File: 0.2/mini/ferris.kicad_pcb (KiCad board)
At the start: 2 copper layers, 208.8 x 86.8 mm, 114 parts, among them J1 USB C, K0_0 KEYSW, K0_1 KEYSW, K0_2 KEYSW, K0_3 KEYSW, K0_4 KEYSW, K0_5 KEYSW, K0_6 KEYSW, K0_7 KEYSW, K0_8 KEYSW, K0_9 KEYSW, K1_0 KEYSW, K1_1 KEYSW, K1_2 KEYSW, K1_3 KEYSW, K1_4 KEYSW, K1_5 KEYSW, K1_6 KEYSW, K1_7 KEYSW, K1_8 KEYSW, K1_9 KEYSW, K2_0 KEYSW, K2_1 KEYSW, K2_2 KEYSW, K2_3 KEYSW, K2_4 KEYSW, K2_5 KEYSW, K2_6 KEYSW, K2_7 KEYSW, K2_8 KEYSW, K2_9 KEYSW, K3_3 KEYSW, K3_4 KEYSW, K3_5 KEYSW, K3_6 KEYSW, Q1 DTC123J, SW1 SW_PUSH, U1 STM32F072CBTx, U2 MCP23017_SO, U3 MCP1700-3302E_SOT23, U4 SRV05-4

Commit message: Remove last few references to ferris.pretty and the entire directory
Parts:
- removed the mouse-bite-2mm-slot at (132.8, 30.0)
- removed the mouse-bite-2mm-slot at (103.2, 30.0)
- added mouse-bite-2mm-slot: VAL**, panelization:mouse-bite-2mm-slot-with-space-for-track, F.Cu at (132.8, 30.0)
- added mouse-bite-2mm-slot: VAL**, panelization:mouse-bite-2mm-slot-with-space-for-track, F.Cu at (103.2, 30.0)
- G*** (x2): footprint ferris:ducking_ferris_pad -> copper_pads:ferris_low
- REF**: footprint ferris:silk_pg1232_schematic -> silkscreens:pg1232_schematic
- REF**: footprint ferris:silk_pg2132_top -> silkscreens:pg1232_top
- REF**: footprint ferris:silk_pg1232_bottom -> silkscreens:pg1232_bottom
- REF**: footprint ferris:silk_pg1232_right -> silkscreens:pg1232_right
- REF**: footprint ferris:silk_pg1232_left -> silkscreens:pg1232_left
- REF**: footprint ferris:silk_pg1232_footprint -> silkscreens:pg1232_footprint
- REF**: footprint ferris:silk_pg1232_side -> silkscreens:pg1232_side
- mouse-bite-2mm-slot: footprint ferris:mouse-bite-2mm-slot-with-space-for-track -> panelization:mouse-bite-2mm-slot-with-space-for-track

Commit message: 0.2/mini: Add human readable "Part Name" field
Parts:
- C12, C13: value 0.1u -> 0.1uF
- D0_0, D0_1, D0_2, D0_3, D0_4, D0_5, D0_6, D0_7, D0_8, D0_9, D1_0, D1_1, D1_2, D1_3, D1_4, D1_5, D1_6, D1_7, D1_8, D1_9, D2_0, D2_1, D2_2, D2_3, D2_4, D2_5, D2_6, D2_7, D2_8, D2_9, D3, D3_3, D3_4, D3_5, D3_6: value D -> 1N4148W
- J1: value USB C -> TYPE-C-31-M-12
- Jack0, Jack1: value TRRS -> PJ-320A
- Q1: value DTC123J -> PDTC123JT,215
- R1, R2: value 5.1K -> 5.1kΩ
- R3, R4, R5: value 100k -> 100kΩ
- R6: value 10k -> 10kΩ
- R7, R8: value 4.7k -> 4.7kΩ
- SW1: value SW_PUSH -> B3U-1000P
- U1: value STM32F072CBTx -> STM32F072CBT6
- U2: value MCP23017_SO -> MCP23017-E/SO
- U3: value MCP1700-3302E_SOT23 -> MCP1700T-3302E/TT
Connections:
- J1 pad A8: (no net) -> Net-(J1-PadA8)
- J1 pad B8: (no net) -> Net-(J1-PadB8)
- U2 pad 11: (no net) -> Net-(U2-Pad11)
- U2 pad 14: (no net) -> Net-(U2-Pad14)
- U2 pad 19: (no net) -> Net-(U2-Pad19)
- U2 pad 20: (no net) -> Net-(U2-Pad20)
- U2 pad 26: (no net) -> Net-(U2-Pad26)
- U2 pad 27: (no net) -> Net-(U2-Pad27)
- U2 pad 28: (no net) -> Net-(U2-Pad28)
- U2 pad 5: (no net) -> Net-(U2-Pad5)
- U2 pad 6: (no net) -> Net-(U2-Pad6)
- U2 pad 7: (no net) -> Net-(U2-Pad7)
- U2 pad 8: (no net) -> Net-(U2-Pad8)

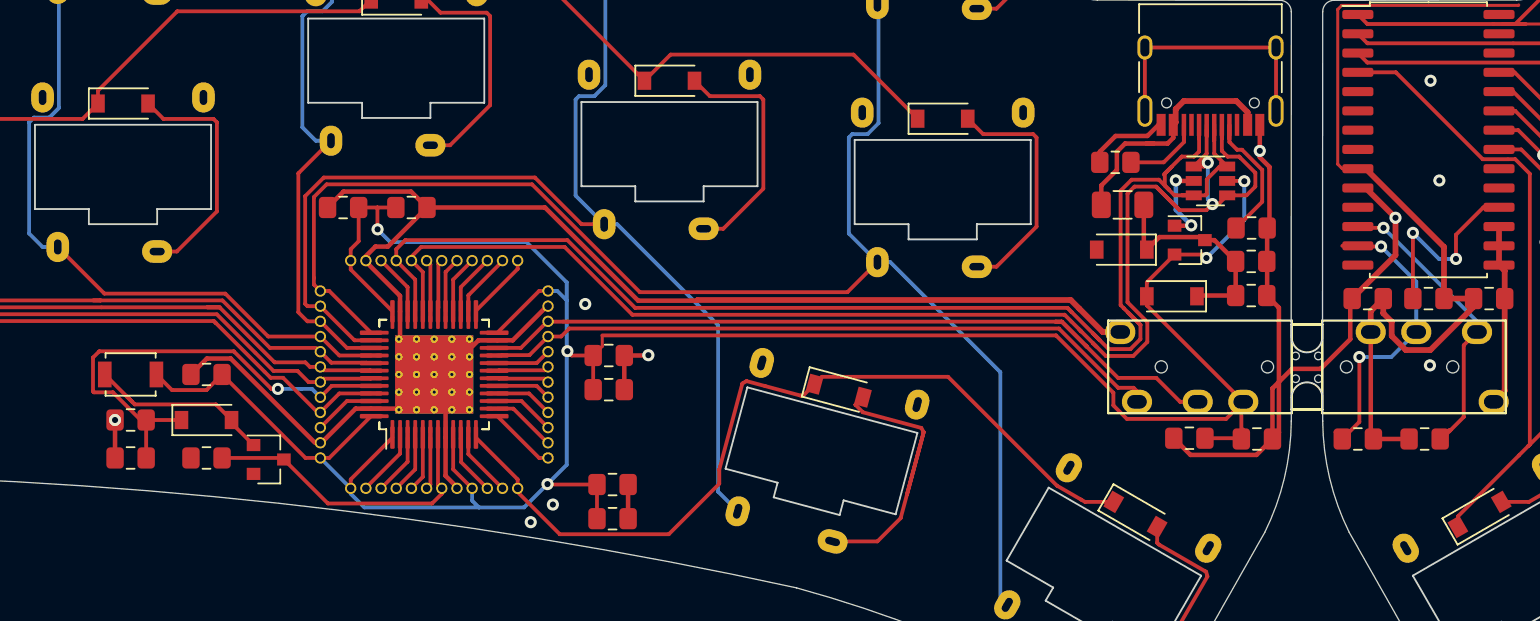
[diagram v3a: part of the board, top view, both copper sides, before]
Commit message: Ferris mini: Update PCB to ease case design
Perform a number of small changes to allow for creation of a symmetrical
switch plate that can cover the MCU area and leave the USB area exposed.
Also move components a bit further from the switches to avoid very slim
parts of the case.

* Move reset button to USB area
* Layout the USB area in a more compact way
* Bring MCU's decoupling capacitors closer to the MCU
* Bring Components under the Jack plugs closer to each other
* Reroute traces accordingly
* Update version to 0.2.1 to reflect the change (silk and mini card)
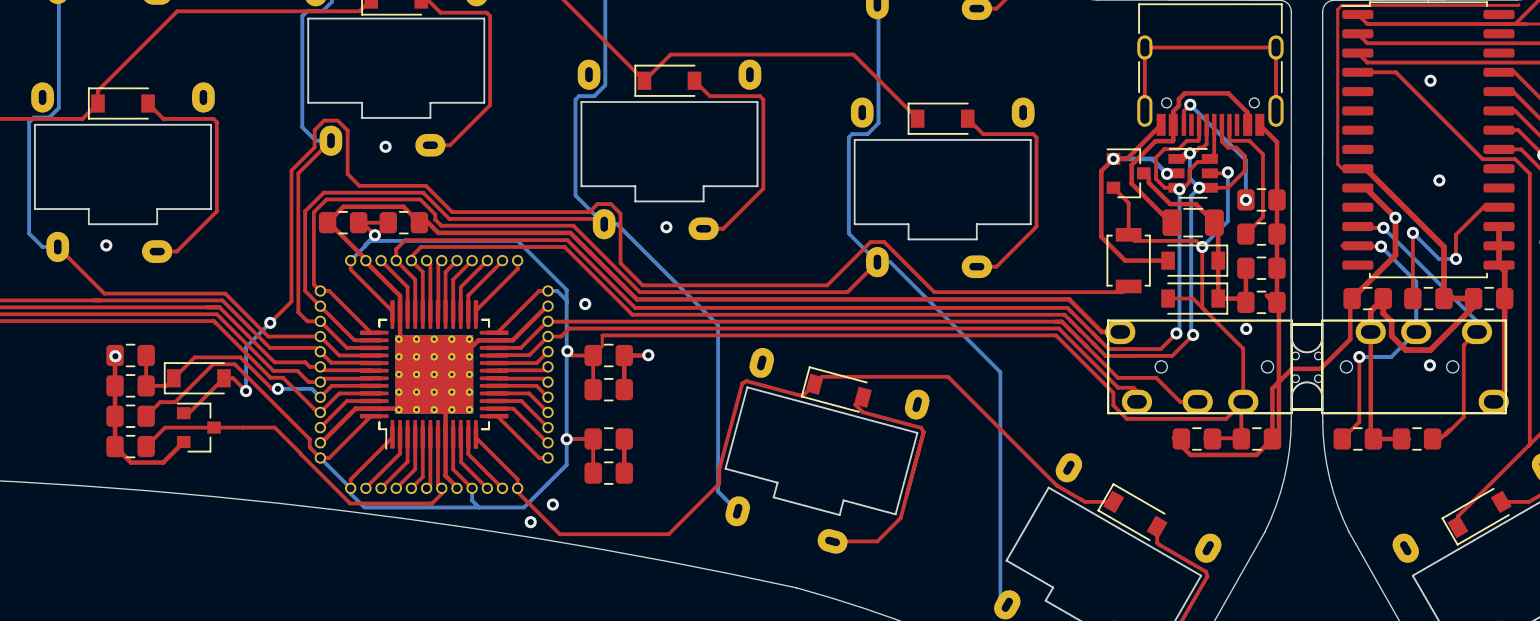
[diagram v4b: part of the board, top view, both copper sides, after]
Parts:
- moved SW1 66.2 mm to (106.2, 69.0), turned to 270 degrees
- moved R2 9.94 mm to (115.0, 65.0), turned to 180 degrees
- moved R5 6.75 mm to (40.5, 75.2)
- moved U3 5.96 mm to (106.2, 63.2)
- moved C9 5.71 mm to (40.5, 79.2)
- moved Q1 5.06 mm to (45.0, 80.0)
- moved C4 5.06 mm to (40.5, 81.2)
- moved F1 4.80 mm to (110.5, 66.5)
- moved D1 4.76 mm to (110.5, 69.0)
- moved C7 3.01 mm to (72.0, 80.8)
- moved C8 3.01 mm to (72.0, 83.0)
- moved D3 2.80 mm to (45.0, 76.8)
- moved C3 2.25 mm to (40.5, 77.2)
- moved D2 1.41 mm to (110.5, 71.5)
- moved U4 1.24 mm to (110.5, 63.2)
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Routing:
- net Net-(D3-Pad2): track 12.3 -> 89.6 mm, vias 0 -> 2
- net BOOT0: track 31.4 -> 19.4 mm
- net /D-: track 92.8 -> 84.1 mm, vias 2 -> 3
- net /D+: track 90.3 -> 83.4 mm, vias 0 -> 2
- net +3V3: track 176.5 -> 182.9 mm
- net NRST: track 20.0 -> 25.9 mm
- net GND: track 214.4 -> 218.9 mm, vias 25 -> 28
- net Net-(J1-PadB5): track 6.18 -> 9.29 mm, vias 0 -> 2
- net /col3: track 95.7 -> 94.1 mm
- net /col4: track 117.1 -> 115.9 mm
- net VCC: track 16.5 -> 17.2 mm
- net +5V: track 14.7 -> 15.4 mm
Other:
- board text added: "Ferris Mini - v0.2.1 by @pierrec83 As low profile as it gets! * Split, 34 Keys * Kailh Choc Mini: pg1232 * Choc spacing: 17x18mm * Microcontroller: STM32FO72 * IO Expander: MCP23017 * USB C * All mcu pins broken out * Dimensions: 104x87mm per side Fully open source design: github.com/pierrechevalier83/ferris"
- board text added: "Ferris Mini v0.2.1"
- board text removed: "Ferris Mini - v0.2 by @pierrec83 As low profile as it gets! * Split, 34 Keys * Kailh Choc Mini: pg1232 * Choc spacing: 17x18mm * Microcontroller: STM32FO72 * IO Expander: MCP23017 * USB C * All mcu pins broken out * Dimensions: 104x87mm per side Fully open source design: github.com/pierrechevalier83/ferris"
- board text removed: "Ferris Mini v0.2"
